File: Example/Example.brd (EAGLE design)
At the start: 86 x 54 mm, 10 parts, among them IC1 LM555D, J1 UX60-MB-5S8, SW1 MFS101D-6-Z

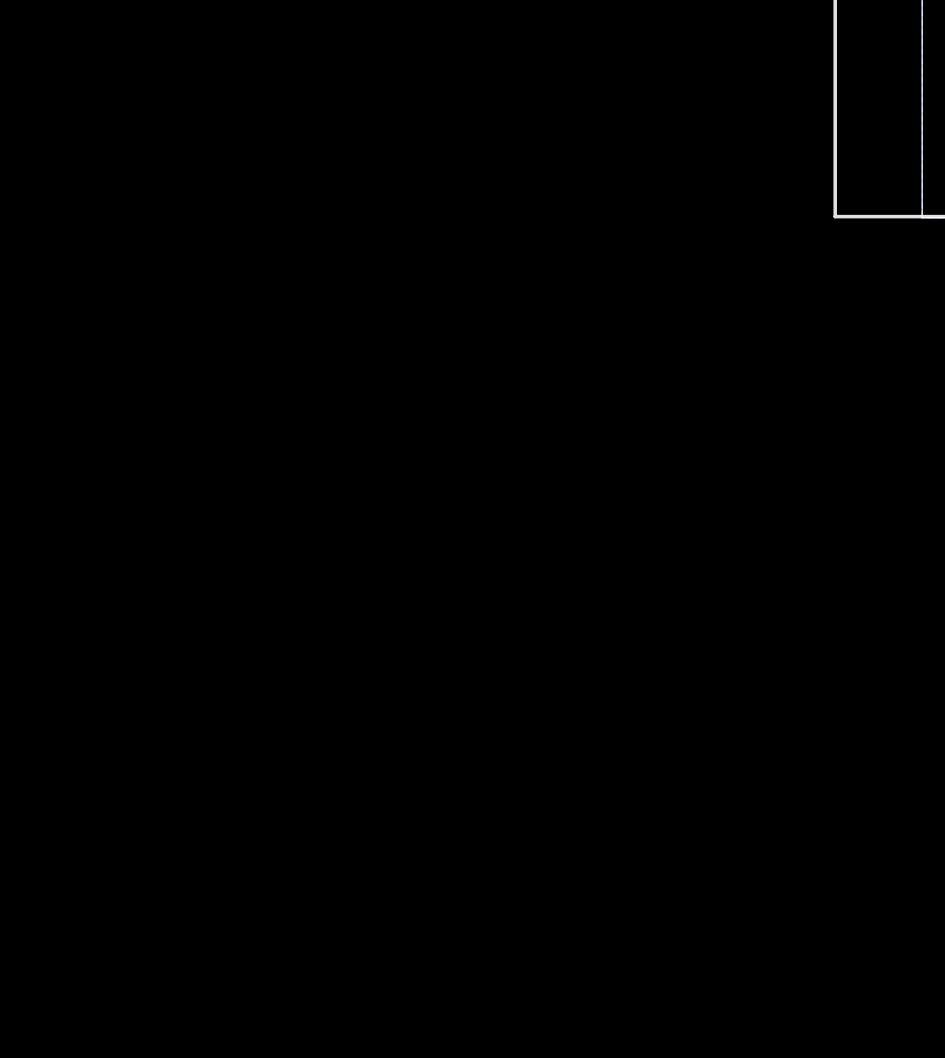
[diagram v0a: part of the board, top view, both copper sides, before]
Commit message: added four new parts
added button, cell, led, and nor gate
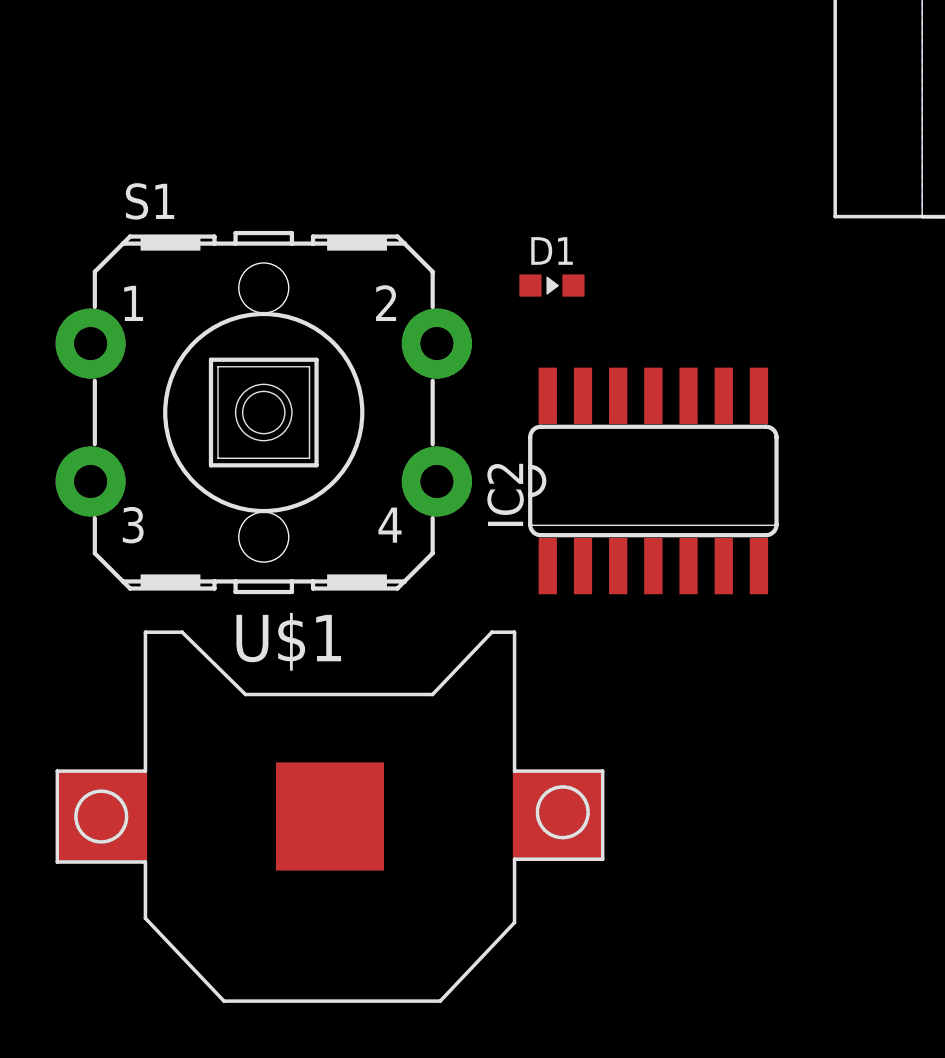
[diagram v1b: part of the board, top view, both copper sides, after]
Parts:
- added D1: YELLOW, RoboJackets-LEDs:LED0603
- added IC2: 74LS02D, 74xx-us:SO14
- added S1: (no value), adafruit:B3F-40XX-ROUND
- added U$1: (no value), adafruit:CR1220-SMD
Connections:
- new net VCC: IC2.14
- net GND: now also IC2.7
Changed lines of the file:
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@@
 <?xml version="1.0" encoding="utf-8"?>
 <!DOCTYPE eagle SYSTEM "eagle.dtd">
-<eagle version="9.5.1">
+<eagle version="9.5.2">
 <drawing>
 <settings>
@@
 <attribute name="DKPN" value="563-1555-ND" x="4.8" y="19.57" size="1.778" layer="27" rot="R90" display="off"/>
 </element>
+<element name="D1" library="RoboJackets-LEDs" package="LED0603" value="YELLOW" x="-13.36" y="-2.45" smashed="yes">
+<attribute name="DKPN" value="160-1448-1-ND" x="-13.36" y="-2.45" size="1.778" layer="27" display="off"/>
+<attribute name="NAME" x="-13.36" y="-1.7" size="1" layer="25" font="vector" ratio="10" align="bottom-center"/>
+<attribute name="VALUE" x="-13.36" y="-3.2" size="1" layer="27" font="vector" ratio="10" align="top-center"/>
+</element>
+<element name="IC2" library="74xx-us" library_urn="urn:adsk.eagle:library:88" package="SO14" package3d_urn="urn:adsk.eagle:package:2917/1" value="74LS02D" x="-9.7" y="-9.5" smashed="yes">
+<attribute name="NAME" x="-14.399" y="-11.278" size="1.27" layer="25" ratio="10" rot="R90"/>
+<attribute name="POPULARITY" value="0" x="-9.7" y="-9.5" size="1.778" layer="27" display="off"/>
+<attribute name="VALUE" x="-13.256" y="-10.008" size="1.27" layer="27" ratio="10"/>
+</element>
+<element name="S1" library="adafruit" library_urn="urn:adsk.eagle:library:420" package="B3F-40XX-ROUND" package3d_urn="urn:adsk.eagle:package:6240926/1" value="" x="-23.76" y="-7.03" smashed="yes">
+<attribute name="NAME" x="-28.84" y="-0.045" size="1.27" layer="25" ratio="10"/>
+<attribute name="VALUE" x="-26.935" y="-12.11" size="1.27" layer="27" ratio="10"/>
+</element>
+<element name="U$1" library="adafruit" library_urn="urn:adsk.eagle:library:420" package="CR1220-SMD" package3d_urn="urn:adsk.eagle:package:6240665/1" value="" x="-21.37" y="-21.61" smashed="yes">
+<attribute name="NAME" x="-24.926" y="-16.008" size="1.6764" layer="25" font="vector"/>
+<attribute name="VALUE" x="-25.688" y="-26.16" size="1.6764" layer="27" font="vector"/>
+</element>
 </elements>
 <signals>
@@
 <wire x1="15.877" y1="13.783" x2="16.17" y2="13.49" width="0.2" layer="1"/>
 <via x="16.17" y="13.49" extent="1-16" drill="0.35"/>
+<contactref element="IC2" pad="7"/>
 <wire x1="10.06" y1="24.08" x2="9.58" y2="32.46" width="0" layer="19" extent="1-1"/>
 <wire x1="13.11" y1="24.29" x2="11.5" y2="23.43" width="0" layer="19" extent="1-1"/>
@@
 <wire x1="14.105" y1="11.66" x2="14.105" y2="13.783" width="0" layer="19" extent="1-1"/>
 <wire x1="4.562" y1="4.54" x2="13.54" y2="9.9" width="0" layer="19" extent="1-1"/>
+<wire x1="-5.89" y1="-12.5734" x2="4.562" y2="4.54" width="0" layer="19" extent="1-1"/>
 </signal>
 <signal name="+9V">
@@
 <contactref element="SW1" pad="1"/>
 </signal>
+<signal name="VCC">
+<contactref element="IC2" pad="14"/>
+</signal>
 </signals>

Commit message: sr latch
finished sr latch
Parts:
- removed D1: YELLOW, RoboJackets-LEDs:LED0603
- added D2, D3: YELLOW, RoboJackets-LEDs:LED0603
- added IC3: 74LS02D, 74xx-us:SO14
- added R1, R2, R3: (no value), rcl:R0603
- added S2: (no value), adafruit:B3F-40XX-ROUND
- added U$3: (no value), adafruit:CR1220-SMD
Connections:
- new net N$2: D3.A
- new net N$5: D3.C, R3.2
- new net Q: IC2.1, IC3.2
- new net QNOT: IC2.3, IC3.1
- new net R: IC2.2, R1.2, S1.2
- new net S: IC3.3, R2.2, S2.2
- net GND: now also IC3.7, R1.1, R2.1, R3.1, U$1.-, U$3.-
- net VCC: now also IC3.14, S1.3, S2.3, U$1.+$1, U$3.+$1
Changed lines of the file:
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@@
 <?xml version="1.0" encoding="utf-8"?>
 <!DOCTYPE eagle SYSTEM "eagle.dtd">
-<eagle version="9.5.2">
+<eagle version="9.5.1">
 <drawing>
 <settings>
@@
 <attribute name="DKPN" value="563-1555-ND" x="4.8" y="19.57" size="1.778" layer="27" rot="R90" display="off"/>
 </element>
-<element name="D1" library="RoboJackets-LEDs" package="LED0603" value="YELLOW" x="-13.36" y="-2.45" smashed="yes">
-<attribute name="DKPN" value="160-1448-1-ND" x="-13.36" y="-2.45" size="1.778" layer="27" display="off"/>
-<attribute name="NAME" x="-13.36" y="-1.7" size="1" layer="25" font="vector" ratio="10" align="bottom-center"/>
-<attribute name="VALUE" x="-13.36" y="-3.2" size="1" layer="27" font="vector" ratio="10" align="top-center"/>
-</element>
 <element name="IC2" library="74xx-us" library_urn="urn:adsk.eagle:library:88" package="SO14" package3d_urn="urn:adsk.eagle:package:2917/1" value="74LS02D" x="-9.7" y="-9.5" smashed="yes">
 <attribute name="NAME" x="-14.399" y="-11.278" size="1.27" layer="25" ratio="10" rot="R90"/>
@@
 <attribute name="NAME" x="-24.926" y="-16.008" size="1.6764" layer="25" font="vector"/>
 <attribute name="VALUE" x="-25.688" y="-26.16" size="1.6764" layer="27" font="vector"/>
+</element>
+<element name="IC3" library="74xx-us" library_urn="urn:adsk.eagle:library:88" package="SO14" package3d_urn="urn:adsk.eagle:package:2917/1" value="74LS02D" x="-10.37" y="-33.07" smashed="yes">
+<attribute name="NAME" x="-15.069" y="-34.848" size="1.27" layer="25" ratio="10" rot="R90"/>
+<attribute name="POPULARITY" value="0" x="-10.37" y="-33.07" size="1.778" layer="27" display="off"/>
+<attribute name="VALUE" x="-13.926" y="-33.578" size="1.27" layer="27" ratio="10"/>
+</element>
+<element name="D2" library="RoboJackets-LEDs" package="LED0603" value="YELLOW" x="-28.4" y="-39.58" smashed="yes">
+<attribute name="DKPN" value="160-1448-1-ND" x="-28.4" y="-39.58" size="1.778" layer="27" display="off"/>
+<attribute name="NAME" x="-28.4" y="-38.83" size="1" layer="25" font="vector" ratio="10" align="bottom-center"/>
+<attribute name="VALUE" x="-28.4" y="-40.33" size="1" layer="27" font="vector" ratio="10" align="top-center"/>
+</element>
+<element name="D3" library="RoboJackets-LEDs" package="LED0603" value="YELLOW" x="-28.4" y="-43.86" smashed="yes">
+<attribute name="DKPN" value="160-1448-1-ND" x="-28.4" y="-43.86" size="1.778" layer="27" display="off"/>
+<attribute name="NAME" x="-28.4" y="-43.11" size="1" layer="25" font="vector" ratio="10" align="bottom-center"/>
+<attribute name="VALUE" x="-28.4" y="-44.61" size="1" layer="27" font="vector" ratio="10" align="top-center"/>
+</element>
+<element name="R1" library="rcl" library_urn="urn:adsk.eagle:library:334" package="R0603" package3d_urn="urn:adsk.eagle:package:23555/3" value="" x="-29.78" y="-48.41" smashed="yes">
+<attribute name="NAME" x="-30.415" y="-47.775" size="1.27" layer="25"/>
+<attribute name="POPULARITY" value="77" x="-29.78" y="-48.41" size="1.778" layer="27" display="off"/>
+<attribute name="SPICEPREFIX" value="R" x="-29.78" y="-48.41" size="1.778" layer="27" display="off"/>
+<attribute name="VALUE" x="-30.415" y="-50.315" size="1.27" layer="27"/>
+</element>
+<element name="S2" library="adafruit" library_urn="urn:adsk.eagle:library:420" package="B3F-40XX-ROUND" package3d_urn="urn:adsk.eagle:package:6240926/1" value="" x="-23.76" y="-58.24" smashed="yes">
+<attribute name="NAME" x="-28.84" y="-51.255" size="1.27" layer="25" ratio="10"/>
+<attribute name="VALUE" x="-26.935" y="-63.32" size="1.27" layer="27" ratio="10"/>
+</element>
+<element name="R2" library="rcl" library_urn="urn:adsk.eagle:library:334" package="R0603" package3d_urn="urn:adsk.eagle:package:23555/3" value="" x="-29.78" y="-67.26" smashed="yes">
+<attribute name="NAME" x="-30.415" y="-66.625" size="1.27" layer="25"/>
+<attribute name="POPULARITY" value="77" x="-44.82" y="-51.89" size="1.778" layer="27" display="off"/>
+<attribute name="SPICEPREFIX" value="R" x="-44.82" y="-51.89" size="1.778" layer="27" display="off"/>
+<attribute name="VALUE" x="-30.415" y="-69.165" size="1.27" layer="27"/>
+</element>
+<element name="R3" library="rcl" library_urn="urn:adsk.eagle:library:334" package="R0603" package3d_urn="urn:adsk.eagle:package:23555/3" value="" x="-29.78" y="-70.74" smashed="yes">
+<attribute name="NAME" x="-30.415" y="-70.105" size="1.27" layer="25"/>
+<attribute name="POPULARITY" value="77" x="-29.78" y="-70.74" size="1.778" layer="27" display="off"/>
+<attribute name="SPICEPREFIX" value="R" x="-29.78" y="-70.74" size="1.778" layer="27" display="off"/>
+<attribute name="VALUE" x="-30.415" y="-72.645" size="1.27" layer="27"/>
+</element>
+<element name="U$3" library="adafruit" library_urn="urn:adsk.eagle:library:420" package="CR1220-SMD" package3d_urn="urn:adsk.eagle:package:6240665/1" value="" x="-21.37" y="-79.78" smashed="yes">
+<attribute name="NAME" x="-24.926" y="-74.178" size="1.6764" layer="25" font="vector"/>
+<attribute name="VALUE" x="-25.688" y="-84.33" size="1.6764" layer="27" font="vector"/>
 </element>
 </elements>
@@
 <via x="16.17" y="13.49" extent="1-16" drill="0.35"/>
 <contactref element="IC2" pad="7"/>
-<wire x1="10.06" y1="24.08" x2="9.58" y2="32.46" width="0" layer="19" extent="1-1"/>
-<wire x1="13.11" y1="24.29" x2="11.5" y2="23.43" width="0" layer="19" extent="1-1"/>
-<wire x1="20.2944" y1="15.719" x2="14.546" y2="23.495" width="0" layer="19" extent="1-1"/>
-<wire x1="16.17" y1="13.49" x2="20.2944" y2="15.719" width="0" layer="19" extent="1-1"/>
-<wire x1="14.105" y1="11.66" x2="14.105" y2="13.783" width="0" layer="19" extent="1-1"/>
-<wire x1="4.562" y1="4.54" x2="13.54" y2="9.9" width="0" layer="19" extent="1-1"/>
-<wire x1="-5.89" y1="-12.5734" x2="4.562" y2="4.54" width="0" layer="19" extent="1-1"/>
+<contactref element="IC3" pad="7"/>
+<contactref element="R1" pad="1"/>
+<contactref element="R2" pad="1"/>
+<contactref element="R3" pad="1"/>
+<contactref element="U$1" pad="-"/>
+<contactref element="U$3" pad="-"/>
+<wire x1="-30.63" y1="-67.26" x2="-30.63" y2="-70.74" width="0" layer="19" extent="1-1"/>
+<wire x1="-21.37" y1="-79.78" x2="-30.63" y2="-70.74" width="0" layer="19" extent="1-1"/>
+<wire x1="-30.63" y1="-48.41" x2="-30.63" y2="-67.26" width="0" layer="19" extent="1-1"/>
+<wire x1="-6.56" y1="-36.1434" x2="-30.63" y2="-48.41" width="0" layer="19" extent="1-1"/>
+<wire x1="-21.37" y1="-21.61" x2="-6.56" y2="-36.1434" width="0" layer="19" extent="1-1"/>
+<wire x1="-5.89" y1="-12.5734" x2="-21.37" y2="-21.61" width="0" layer="19" extent="1-1"/>
+<wire x1="4.562" y1="4.54" x2="-5.89" y2="-12.5734" width="0" layer="19" extent="1-1"/>
+<wire x1="13.54" y1="9.9" x2="4.562" y2="4.54" width="0" layer="19" extent="1-1"/>
+<wire x1="14.105" y1="13.783" x2="14.105" y2="11.66" width="0" layer="19" extent="1-1"/>
+<wire x1="20.2944" y1="15.719" x2="16.17" y2="13.49" width="0" layer="19" extent="1-1"/>
+<wire x1="14.546" y1="23.495" x2="20.2944" y2="15.719" width="0" layer="19" extent="1-1"/>
+<wire x1="11.5" y1="23.43" x2="13.11" y2="24.29" width="0" layer="19" extent="1-1"/>
+<wire x1="9.58" y1="32.46" x2="10.06" y2="24.08" width="0" layer="19" extent="1-1"/>
 </signal>
 <signal name="+9V">
@@
 <signal name="VCC">
 <contactref element="IC2" pad="14"/>
+<contactref element="IC3" pad="14"/>
+<contactref element="S1" pad="3"/>
+<contactref element="S2" pad="3"/>
+<contactref element="U$1" pad="+$1"/>
+<contactref element="U$3" pad="+$1"/>
+<wire x1="-30.0084" y1="-60.7292" x2="-29.57" y2="-79.78" width="0" layer="19" extent="1-1"/>
+<wire x1="-14.18" y1="-29.9966" x2="-30.0084" y2="-60.7292" width="0" layer="19" extent="1-1"/>
+<wire x1="-29.57" y1="-21.61" x2="-14.18" y2="-29.9966" width="0" layer="19" extent="1-1"/>
+<wire x1="-30.0084" y1="-9.5192" x2="-29.57" y2="-21.61" width="0" layer="19" extent="1-1"/>
+<wire x1="-13.51" y1="-6.4266" x2="-30.0084" y2="-9.5192" width="0" layer="19" extent="1-1"/>
+</signal>
+<signal name="QNOT">
+<contactref element="IC2" pad="3"/>
+<contactref element="IC3" pad="1"/>
+<wire x1="-10.97" y1="-12.5734" x2="-14.18" y2="-36.1434" width="0" layer="19" extent="1-1"/>
+</signal>
+<signal name="R">
+<contactref element="IC2" pad="2"/>
+<contactref element="S1" pad="2"/>
+<contactref element="R1" pad="2"/>
+<wire x1="-12.24" y1="-12.5734" x2="-28.93" y2="-48.41" width="0" layer="19" extent="1-1"/>
+<wire x1="-17.5116" y1="-4.5408" x2="-12.24" y2="-12.5734" width="0" layer="19" extent="1-1"/>
+</signal>
+<signal name="Q">
+<contactref element="IC3" pad="2"/>
+<contactref element="IC2" pad="1"/>
+<wire x1="-13.51" y1="-12.5734" x2="-12.91" y2="-36.1434" width="0" layer="19" extent="1-1"/>
+</signal>
+<signal name="S">
+<contactref element="IC3" pad="3"/>
+<contactref element="S2" pad="2"/>
+<contactref element="R2" pad="2"/>
+<wire x1="-17.5116" y1="-55.7508" x2="-28.93" y2="-67.26" width="0" layer="19" extent="1-1"/>
+<wire x1="-11.64" y1="-36.1434" x2="-17.5116" y2="-55.7508" width="0" layer="19" extent="1-1"/>
+</signal>
+<signal name="N$2">
+<contactref element="D3" pad="A"/>
+</signal>
+<signal name="N$5">
+<contactref element="D3" pad="C"/>
+<contactref element="R3" pad="2"/>
+<wire x1="-27.625" y1="-43.86" x2="-28.93" y2="-70.74" width="0" layer="19" extent="1-1"/>
 </signal>
 </signals>

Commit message: Fixed issue of second NOR gate. However, did not delete second NOR gate.
I could not change the attributes of the NOR gates.
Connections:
- new net N$7: IC2.5
- new net N$8: IC2.4
- new net N$9: IC2.6
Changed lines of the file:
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@@
 <?xml version="1.0" encoding="utf-8"?>
 <!DOCTYPE eagle SYSTEM "eagle.dtd">
-<eagle version="9.5.1">
+<eagle version="9.5.2">
 <drawing>
 <settings>
@@
 <attribute name="NAME" x="-14.399" y="-11.278" size="1.27" layer="25" ratio="10" rot="R90"/>
 <attribute name="POPULARITY" value="0" x="-9.7" y="-9.5" size="1.778" layer="27" display="off"/>
+<attribute name="SPICEPREFIX" value="J" x="-9.7" y="-9.5" size="1.778" layer="27" display="off"/>
 <attribute name="VALUE" x="-13.256" y="-10.008" size="1.27" layer="27" ratio="10"/>
 </element>
@@
 <wire x1="-27.625" y1="-43.86" x2="-28.93" y2="-70.74" width="0" layer="19" extent="1-1"/>
 </signal>
+<signal name="N$7">
+<contactref element="IC2" pad="5"/>
+</signal>
+<signal name="N$8">
+<contactref element="IC2" pad="4"/>
+</signal>
+<signal name="N$9">
+<contactref element="IC2" pad="6"/>
+</signal>
 </signals>
